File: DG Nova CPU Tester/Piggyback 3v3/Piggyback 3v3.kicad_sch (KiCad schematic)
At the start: 15 parts, among them J10 Programmed I/O, J11 CPU Option Inputs, J12 Data Channel, J13 Program Interrupt, J14 System Control, J17 CPU Option Outputs, J18 MEM Control Outputs, J19 Logic 8 CH, J20 Logic 8 CH, J6 MBO, J7 MEM, J8 Data Channel, J9 Front Panel Controls, U2 Pico

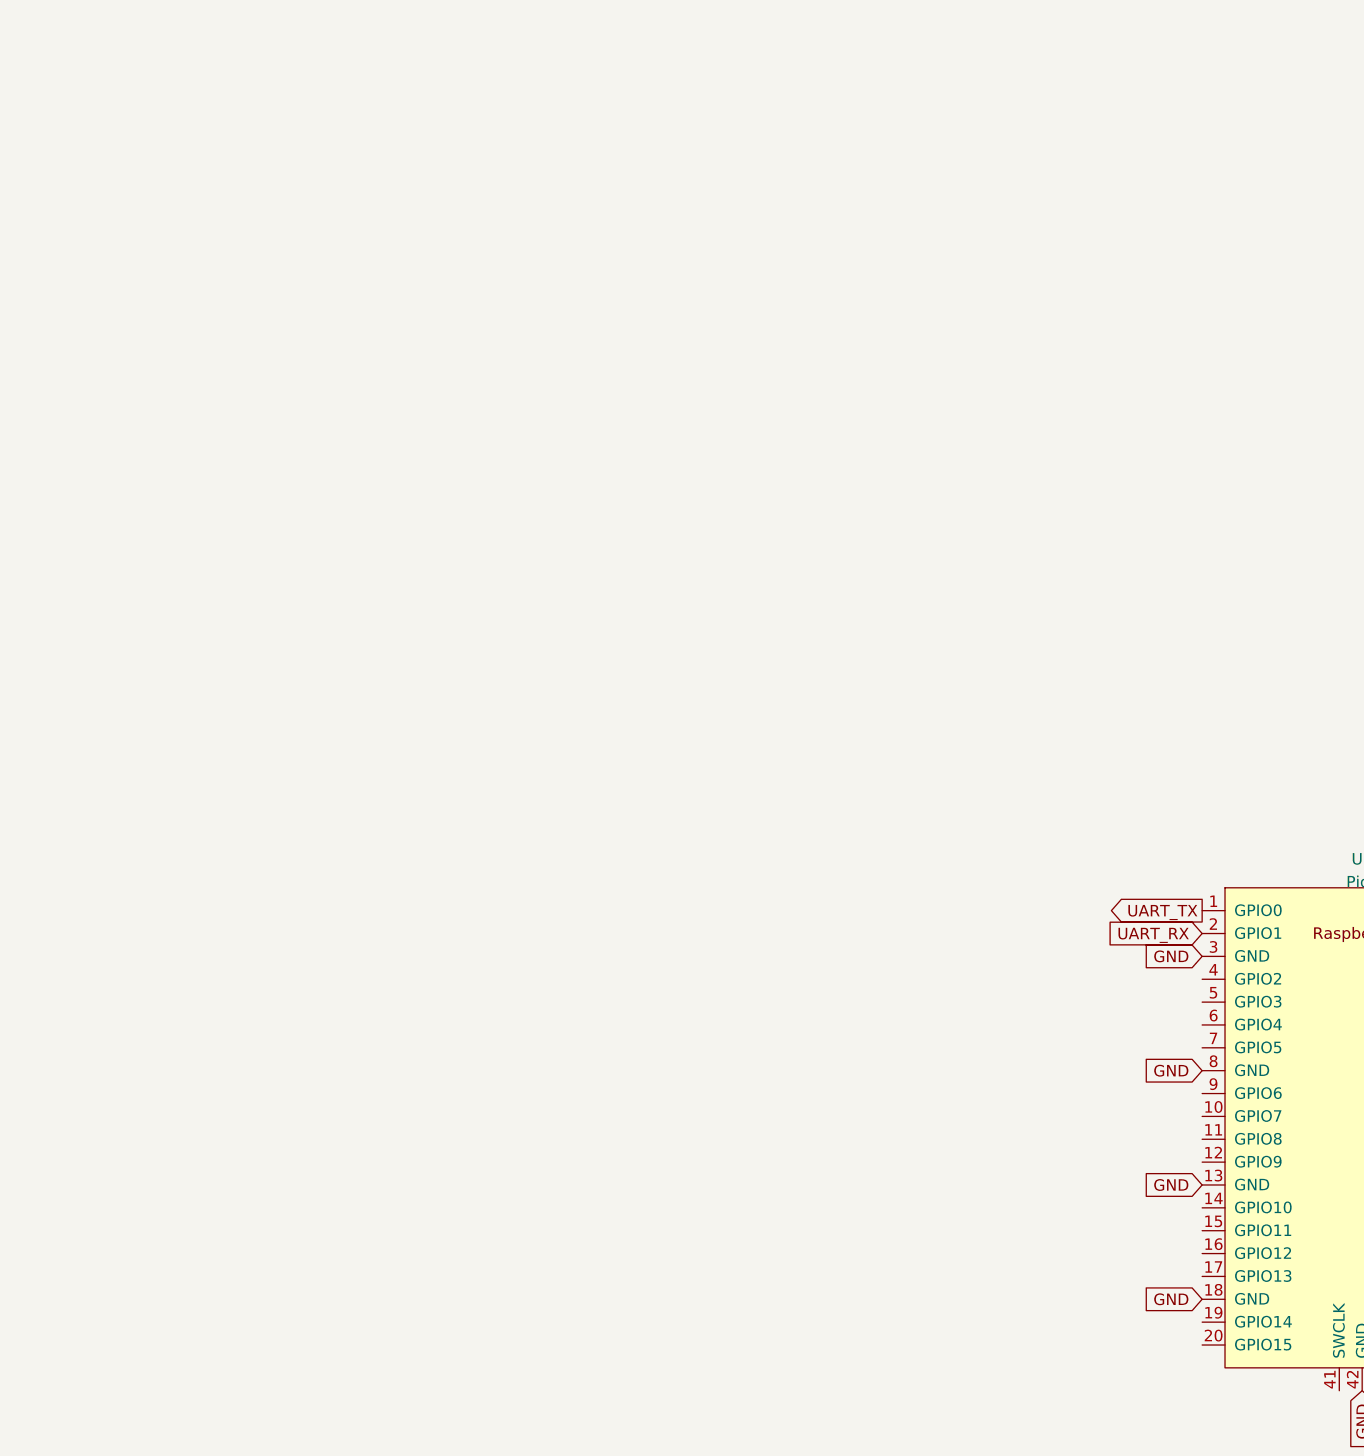
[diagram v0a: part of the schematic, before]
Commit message: Some DRC Cleanup, add 3v3 to back board
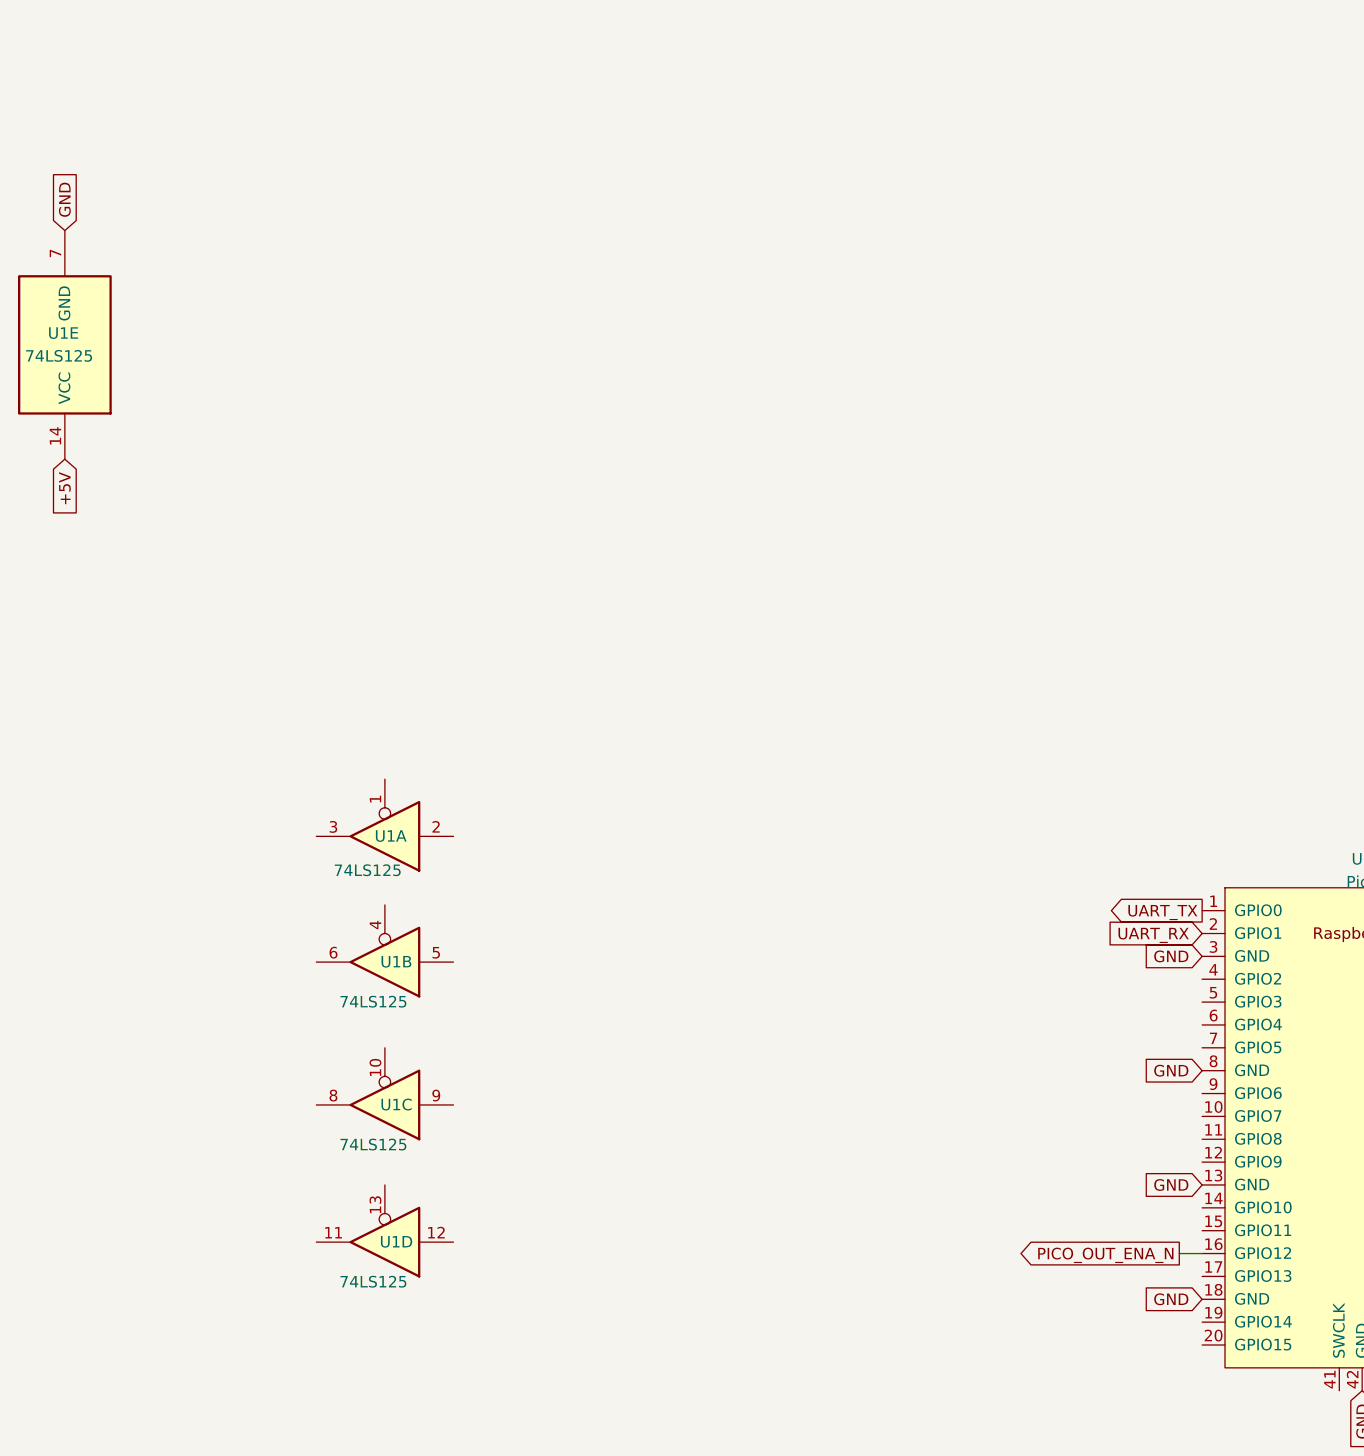
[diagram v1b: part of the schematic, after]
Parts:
- added U1: 74LS125, symbol 74xx:74LS125
- U2: footprint Forgotten Machines:RPi_Pico_SMD_TH -> Forgotten Machines:RPi_Pico_SMD_TH - Backside Silkscreen Frontside Mount
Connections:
- net +5V: now also U1.14 (VCC)
- net GND: now also U1.7 (GND)
- net PICO_OUT_ENA_N: now reaches U2.16 (GPIO12)
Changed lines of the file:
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@@
 (kicad_sch (version 20230121) (generator eeschema)
   (paper "User" 499.999 599.999)
+  (wire (pts (xy 85.09 220.345) (xy 87.63 220.345))
+    (stroke (width 0) (type default))
+  )
   (rectangle (start 130.81 66.04) (end 172.72 15.875)
     (stroke (width 0) (type default))
@@
     )
   )
+  (global_label "PICO_OUT_ENA_N" (shape output) (at 85.09 220.345 180) (fields_autoplaced)
+    (effects (font (size 1.27 1.27)) (justify right))
+    (property "Intersheetrefs" "${INTERSHEET_REFS}" (at 66.7717 220.2656 0)
+      (effects (font (size 1.27 1.27)) (justify right) hide)
+    )
+  )
   (global_label "~{MEM11}" (shape input) (at 79.375 50.8 0) (fields_autoplaced)
     (effects (font (size 1.27 1.27)) (justify left))
@@
     )
   )
+  (global_label "GND" (shape input) (at -38.735 106.68 90) (fields_autoplaced)
+    (effects (font (size 1.27 1.27)) (justify left))
+    (property "Intersheetrefs" "${INTERSHEET_REFS}" (at -38.735 100.4785 90)
+      (effects (font (size 1.27 1.27)) (justify left) hide)
+    )
+  )
   (global_label "~{INH TRANS}" (shape input) (at 106.68 47.625 0) (fields_autoplaced)
     (effects (font (size 1.27 1.27)) (justify left))
@@
     )
   )
+  (global_label "+5V" (shape input) (at -38.735 132.08 270) (fields_autoplaced)
+    (effects (font (size 1.27 1.27)) (justify right))
+    (property "Intersheetrefs" "${INTERSHEET_REFS}" (at -38.735 138.2815 90)
+      (effects (font (size 1.27 1.27)) (justify right) hide)
+    )
+  )
   (symbol (lib_id "Connector_Generic:Conn_01x16") (at 66.04 40.64 0) (unit 1)
     (in_bom yes) (on_board yes) (dnp no)
@@
     )
   )
+  (symbol (lib_id "74xx:74LS125") (at -38.735 119.38 180) (unit 5)
+    (in_bom yes) (on_board yes) (dnp no)
+    (property "Reference" "U1" (at -40.64 118.11 0)
+      (effects (font (size 1.27 1.27)) (justify right))
+    )
+    (property "Value" "74LS125" (at -43.18 120.65 0)
+      (effects (font (size 1.27 1.27)) (justify right))
+    )
+    (property "Footprint" "" (at -38.735 119.38 0)
+      (effects (font (size 1.27 1.27)) hide)
+    )
+    (property "Datasheet" "http://www.ti.com/lit/gpn/sn74LS125" (at -38.735 119.38 0)
+      (effects (font (size 1.27 1.27)) hide)
+    )
+    (pin "7")
+    (pin "9")
+    (pin "10")
+    (pin "13")
+    (pin "6")
+    (pin "11")
+    (pin "3")
+    (pin "5")
+    (pin "8")
+    (pin "4")
+    (pin "14")
+    (pin "2")
+    (pin "12")
+    (pin "1")
+    (instances
+      (project "Piggyback 3v3"
+        (path "/c1f710ce-b3f9-4828-9325-9c2326e8d74c"
+          (reference "U1") (unit 5)
+        )
+      )
+    )
+  )
+  (symbol (lib_id "74xx:74LS125") (at -3.175 203.835 180) (unit 3)
+    (in_bom yes) (on_board yes) (dnp no)
+    (property "Reference" "U1" (at -1.905 203.835 0)
+      (effects (font (size 1.27 1.27)))
+    )
+    (property "Value" "74LS125" (at -4.445 208.28 0)
+      (effects (font (size 1.27 1.27)))
+    )
+    (property "Footprint" "" (at -3.175 203.835 0)
+      (effects (font (size 1.27 1.27)) hide)
+    )
+    (property "Datasheet" "http://www.ti.com/lit/gpn/sn74LS125" (at -3.175 203.835 0)
+      (effects (font (size 1.27 1.27)) hide)
+    )
+    (pin "7")
+    (pin "9")
+    (pin "10")
+    (pin "13")
+    (pin "6")
+    (pin "11")
+    (pin "3")
+    (pin "5")
+    (pin "8")
+    (pin "4")
+    (pin "14")
+    (pin "2")
+    (pin "12")
+    (pin "1")
+    (instances
+      (project "Piggyback 3v3"
+        (path "/c1f710ce-b3f9-4828-9325-9c2326e8d74c"
+          (reference "U1") (unit 3)
+        )
+      )
+    )
+  )
   (symbol (lib_id "ForgottenMachines:Teensy4.1") (at 447.04 212.09 0) (unit 1)
     (in_bom yes) (on_board yes) (dnp no) (fields_autoplaced)
@@
     )
   )
+  (symbol (lib_id "74xx:74LS125") (at -3.175 187.96 180) (unit 2)
+    (in_bom yes) (on_board yes) (dnp no)
+    (property "Reference" "U1" (at -1.905 187.96 0)
+      (effects (font (size 1.27 1.27)))
+    )
+    (property "Value" "74LS125" (at -4.445 192.405 0)
+      (effects (font (size 1.27 1.27)))
+    )
+    (property "Footprint" "" (at -3.175 187.96 0)
+      (effects (font (size 1.27 1.27)) hide)
+    )
+    (property "Datasheet" "http://www.ti.com/lit/gpn/sn74LS125" (at -3.175 187.96 0)
+      (effects (font (size 1.27 1.27)) hide)
+    )
+    (pin "7")
+    (pin "9")
+    (pin "10")
+    (pin "13")
+    (pin "6")
+    (pin "11")
+    (pin "3")
+    (pin "5")
+    (pin "8")
+    (pin "4")
+    (pin "14")
+    (pin "2")
+    (pin "12")
+    (pin "1")
+    (instances
+      (project "Piggyback 3v3"
+        (path "/c1f710ce-b3f9-4828-9325-9c2326e8d74c"
+          (reference "U1") (unit 2)
+        )
+      )
+    )
+  )
   (symbol (lib_id "Connector_Generic:Conn_01x16") (at 147.955 41.275 0) (unit 1)
     (in_bom yes) (on_board yes) (dnp no)
@@
       (effects (font (size 1.27 1.27)))
     )
-    (property "Footprint" "Forgotten Machines:RPi_Pico_SMD_TH" (at 105.41 206.375 90)
+    (property "Footprint" "Forgotten Machines:RPi_Pico_SMD_TH - Backside Silkscreen Frontside Mount" (at 105.41 206.375 90)
       (effects (font (size 1.27 1.27)) hide)
     )
@@
     )
   )
+  (symbol (lib_id "74xx:74LS125") (at -3.175 173.99 180) (unit 1)
+    (in_bom yes) (on_board yes) (dnp no)
+    (property "Reference" "U1" (at -2.54 173.99 0)
+      (effects (font (size 1.27 1.27)))
+    )
+    (property "Value" "74LS125" (at -5.08 177.8 0)
+      (effects (font (size 1.27 1.27)))
+    )
+    (property "Footprint" "" (at -3.175 173.99 0)
+      (effects (font (size 1.27 1.27)) hide)
+    )
+    (property "Datasheet" "http://www.ti.com/lit/gpn/sn74LS125" (at -3.175 173.99 0)
+      (effects (font (size 1.27 1.27)) hide)
+    )
+    (pin "7")
+    (pin "9")
+    (pin "10")
+    (pin "13")
+    (pin "6")
+    (pin "11")
+    (pin "3")
+    (pin "5")
+    (pin "8")
+    (pin "4")
+    (pin "14")
+    (pin "2")
+    (pin "12")
+    (pin "1")
+    (instances
+      (project "Piggyback 3v3"
+        (path "/c1f710ce-b3f9-4828-9325-9c2326e8d74c"
+          (reference "U1") (unit 1)
+        )
+      )
+    )
+  )
   (symbol (lib_id "Connector_Generic:Conn_01x06") (at 283.845 29.845 0) (mirror y) (unit 1)
     (in_bom yes) (on_board yes) (dnp no)
@@
         )
       )
+    )
+  )
+  (symbol (lib_id "74xx:74LS125") (at -3.175 219.075 180) (unit 4)
+    (in_bom yes) (on_board yes) (dnp no)
+    (property "Reference" "U1" (at -1.905 219.075 0)
+      (effects (font (size 1.27 1.27)))
+    )
+    (property "Value" "74LS125" (at -4.445 223.52 0)
+      (effects (font (size 1.27 1.27)))
+    )
+    (property "Footprint" "" (at -3.175 219.075 0)
+      (effects (font (size 1.27 1.27)) hide)
+    )
+    (property "Datasheet" "http://www.ti.com/lit/gpn/sn74LS125" (at -3.175 219.075 0)
+      (effects (font (size 1.27 1.27)) hide)
+    )
+    (pin "7")
+    (pin "9")
+    (pin "10")
+    (pin "13")
+    (pin "6")
+    (pin "11")
+    (pin "3")
+    (pin "5")
+    (pin "8")
+    (pin "4")
+    (pin "14")
+    (pin "2")
+    (pin "12")
+    (pin "1")
+    (instances
+      (project "Piggyback 3v3"
+        (path "/c1f710ce-b3f9-4828-9325-9c2326e8d74c"
+          (reference "U1") (unit 4)
+        )
+      )

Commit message: Jumpers & Shottkys
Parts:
- added 3v1: 3v3, Connector_PinHeader_2.54mm:PinHeader_1x04_P2.54mm_Vertical, symbol Connector_Generic:Conn_01x04
- added D1: D_Schottky, Diode_THT:D_DO-35_SOD27_P10.16mm_Horizontal, symbol Device:D_Schottky
- added JP1: Pico 3v3 Power Out, Connector_PinHeader_2.54mm:PinHeader_1x02_P2.54mm_Vertical, symbol Jumper:Jumper_2_Open
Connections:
- net +5V: no longer U2.39 (VSYS)
- net at U2.36 (3V3): now also JP1.1 (A)
- new net: D1.1 (K), U2.39 (VSYS)
- new net +3v3: 3v1.1 (Pin_1), 3v1.2 (Pin_2), 3v1.3 (Pin_3), 3v1.4 (Pin_4), D1.2 (A), JP1.2 (B)
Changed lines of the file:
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@@
 (kicad_sch (version 20230121) (generator eeschema)
   (paper "User" 499.999 599.999)
+  (junction (at 442.595 45.085) (diameter 0) (color 0 0 0 0)
+  )
+  (junction (at 442.595 42.545) (diameter 0) (color 0 0 0 0)
+  )
+  (wire (pts (xy 442.595 45.085) (xy 442.595 47.625))
+    (stroke (width 0) (type default))
+  )
+  (wire (pts (xy 123.19 192.405) (xy 139.7 192.405))
+    (stroke (width 0) (type default))
+  )
   (wire (pts (xy 85.09 220.345) (xy 87.63 220.345))
     (stroke (width 0) (type default))
   )
+  (wire (pts (xy 123.19 184.785) (xy 133.985 184.785))
+    (stroke (width 0) (type default))
+  )
+  (wire (pts (xy 442.595 40.005) (xy 442.595 42.545))
+    (stroke (width 0) (type default))
+  )
+  (wire (pts (xy 442.595 42.545) (xy 442.595 45.085))
+    (stroke (width 0) (type default))
+  )
+  (wire (pts (xy 139.7 192.405) (xy 139.7 195.58))
+    (stroke (width 0) (type default))
+  )
   (rectangle (start 130.81 66.04) (end 172.72 15.875)
     (stroke (width 0) (type default))
@@
     )
   )
-  (global_label "+5V" (shape input) (at 123.19 184.785 0) (fields_autoplaced)
-    (effects (font (size 1.27 1.27)) (justify left))
-    (property "Intersheetrefs" "${INTERSHEET_REFS}" (at 129.3121 184.785 0)
-      (effects (font (size 1.27 1.27)) (justify left) hide)
-    )
-  )
   (global_label "~{READ IO}" (shape input) (at 106.68 27.305 0) (fields_autoplaced)
     (effects (font (size 1.27 1.27)) (justify left))
@@
     )
   )
+  (global_label "+3v3" (shape input) (at 149.86 195.58 0) (fields_autoplaced)
+    (effects (font (size 1.27 1.27)) (justify left))
+    (property "Intersheetrefs" "${INTERSHEET_REFS}" (at 157.15 195.58 0)
+      (effects (font (size 1.27 1.27)) (justify left) hide)
+    )
+  )
   (global_label "~{SHIFT1}" (shape input) (at 261.62 41.91 180) (fields_autoplaced)
     (effects (font (size 1.27 1.27)) (justify right))
@@
     )
   )
+  (global_label "+3v3" (shape input) (at 141.605 184.785 0) (fields_autoplaced)
+    (effects (font (size 1.27 1.27)) (justify left))
+    (property "Intersheetrefs" "${INTERSHEET_REFS}" (at 148.895 184.785 0)
+      (effects (font (size 1.27 1.27)) (justify left) hide)
+    )
+  )
   (global_label "Logic7" (shape input) (at 65.405 306.705 270) (fields_autoplaced)
     (effects (font (size 1.27 1.27)) (justify right))
@@
     )
   )
+  (global_label "+3v3" (shape input) (at 442.595 40.005 180) (fields_autoplaced)
+    (effects (font (size 1.27 1.27)) (justify right))
+    (property "Intersheetrefs" "${INTERSHEET_REFS}" (at 435.305 40.005 0)
+      (effects (font (size 1.27 1.27)) (justify right) hide)
+    )
+  )
   (global_label "~{MEM0}" (shape input) (at 79.375 22.86 0) (fields_autoplaced)
     (effects (font (size 1.27 1.27)) (justify left))
@@
     )
   )
+  (symbol (lib_id "Jumper:Jumper_2_Open") (at 144.78 195.58 0) (unit 1)
+    (in_bom yes) (on_board yes) (dnp no)
+    (property "Reference" "JP1" (at 144.78 189.23 0)
+      (effects (font (size 1.27 1.27)))
+    )
+    (property "Value" "Pico 3v3 Power Out" (at 144.78 191.77 0)
+      (effects (font (size 1.27 1.27)))
+    )
+    (property "Footprint" "Connector_PinHeader_2.54mm:PinHeader_1x02_P2.54mm_Vertical" (at 144.78 195.58 0)
+      (effects (font (size 1.27 1.27)) hide)
+    )
+    (property "Datasheet" "~" (at 144.78 195.58 0)
+      (effects (font (size 1.27 1.27)) hide)
+    )
+    (pin "1")
+    (pin "2")
+    (instances
+      (project "Piggyback 3v3"
+        (path "/c1f710ce-b3f9-4828-9325-9c2326e8d74c"
+          (reference "JP1") (unit 1)
+        )
+      )
+    )
+  )
   (symbol (lib_id "Connector_Generic:Conn_01x10") (at 266.7 34.29 0) (unit 1)
     (in_bom yes) (on_board yes) (dnp no)
@@
     )
   )
+  (symbol (lib_id "Device:D_Schottky") (at 137.795 184.785 0) (unit 1)
+    (in_bom yes) (on_board yes) (dnp no) (fields_autoplaced)
+    (property "Reference" "D1" (at 137.4775 179.07 0)
+      (effects (font (size 1.27 1.27)))
+    )
+    (property "Value" "D_Schottky" (at 137.4775 181.61 0)
+      (effects (font (size 1.27 1.27)))
+    )
+    (property "Footprint" "Diode_THT:D_DO-35_SOD27_P10.16mm_Horizontal" (at 137.795 184.785 0)
+      (effects (font (size 1.27 1.27)) hide)
+    )
+    (property "Datasheet" "~" (at 137.795 184.785 0)
+      (effects (font (size 1.27 1.27)) hide)
+    )
+    (pin "2")
+    (pin "1")
+    (instances
+      (project "Piggyback 3v3"
+        (path "/c1f710ce-b3f9-4828-9325-9c2326e8d74c"
+          (reference "D1") (unit 1)
+        )
+      )
+    )
+  )
   (symbol (lib_id "Connector_Generic:Conn_02x05_Odd_Even") (at 57.785 323.85 0) (unit 1)
     (in_bom yes) (on_board yes) (dnp no)
@@
         )
       )
+    )
+  )
+  (symbol (lib_id "Connector_Generic:Conn_01x04") (at 447.675 42.545 0) (unit 1)
+    (in_bom yes) (on_board yes) (dnp no)
+    (property "Reference" "3v1" (at 445.77 50.165 0)
+      (effects (font (size 1.27 1.27)) (justify left))
+    )
+    (property "Value" "3v3" (at 450.215 45.72 0)
+      (effects (font (size 1.27 1.27)) (justify left) hide)
+    )
+    (property "Footprint" "Connector_PinHeader_2.54mm:PinHeader_1x04_P2.54mm_Vertical" (at 447.675 42.545 0)
+      (effects (font (size 1.27 1.27)) hide)
+    )
+    (property "Datasheet" "~" (at 447.675 42.545 0)
+      (effects (font (size 1.27 1.27)) hide)
+    )
+    (pin "1")
+    (pin "2")
+    (pin "3")
+    (pin "4")
+    (instances
+      (project "Piggyback 3v3"
+        (path "/c1f710ce-b3f9-4828-9325-9c2326e8d74c"
+          (reference "3v1") (unit 1)
+        )
+      )
